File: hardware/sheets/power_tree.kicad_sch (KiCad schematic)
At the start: 0 parts

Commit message: hw: draw Rev A power tree and charger with USB charging state (#5)
* fw: add ICM-42688-P I2C driver

NCS v3.4.1's icm4268x driver supports SPI only, and the Rev A IMU is
wired for I2C. Add a small project driver, packaged as a Zephyr module
under firmware/src/drivers so the application and tests share its
Kconfig, bindings and sources.

The driver reuses the stock register map and devicetree property
encoding, applies the datasheet's I2C settings (I3C SDR/DDR off, slew
rates, SPI interface disabled) and INT_ASYNC_RESET = 0, and supports
data-ready interrupts. Moving the part to SPI only changes the node.

An emulator test on native_sim covers reset and identity checks, the
I2C-mode configuration, unit conversion and the data-ready path. It
does not prove behavior on the real part; wake-on-motion is not
implemented yet.

* hw: add regulator and charger symbols and footprints

Add TPS63802, TPS61023 and BQ25620 symbols with pins and electrical
types from TI's pin tables, and footprints drawn from the manufacturer
land patterns: TI DLA0010A, DRL0006A and RYK0018A (whose L-shaped
corner pads are two pads each), Coilcraft XEL4030 and Murata
DFE201612E.

The TPS63802 body is 2.0 x 3.0 mm per outline 4223750/D; the
datasheet's introductory 1.4 x 2.3 mm figure is out of date.

* hw: draw Rev A power tree and USB charger sheets

Power tree: TPS63802 3.3 V logic rail, TPS61023 LED rail with load
disconnect, switched VBAT measurement, VLED sense, 0-ohm measurement
links and test points. The logic rail is enabled by the power switch
or by the charger's power-good output, so USB starts a charging-only
state with the switch off and removing USB turns the rail off again.
The LED rail and VBAT measurement default off.

Charger: USB-C sink with separate 5.1 kOhm Rd, TPD4E05U06 on D+, D-,
CC1 and CC2, isolated CC sensing, BQ25620 switching charger with BC1.2
detection, a board NTC on TS, and the JST-PH battery header.

The VLED setting is provisional until LED testing. The battery he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
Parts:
- added C201, C203: 10uF 25V, Capacitor_SMD:C_0805_2012Metric, symbol Device:C
- added C202, C204, C205: 22uF 25V, Capacitor_SMD:C_0805_2012Metric, symbol Device:C
- added C206: 4.7nF, Capacitor_SMD:C_0402_1005Metric, symbol Device:C
- added C207, C208: 100nF, Capacitor_SMD:C_0402_1005Metric, symbol Device:C
- added L201: 0.47uH, smart-led-badge:L_Murata_DFE201612E, symbol Device:L
- added L202: 1uH, smart-led-badge:L_Coilcraft_XEL4030, symbol Device:L
- added Q201, Q203: AO3401A, Package_TO_SOT_SMD:SOT-23, symbol Transistor_FET:AO3401A
- added Q202, Q204: AO3400A, Package_TO_SOT_SMD:SOT-23, symbol Transistor_FET:AO3400A
- added R201: 10k, Resistor_SMD:R_0402_1005Metric, symbol Device:R
- added R202, R205: 20k, Resistor_SMD:R_0402_1005Metric, symbol Device:R
- added R203, R208, R214, R219, R222, R223: 100k, Resistor_SMD:R_0402_1005Metric, symbol Device:R
- added R204: 12k, Resistor_SMD:R_0402_1005Metric, symbol Device:R
- added R206, R207: 0, Resistor_SMD:R_0402_1005Metric, symbol Device:R
- added R209, R215: 0, Resistor_SMD:R_0805_2012Metric, symbol Device:R
- added R210: 33k, Resistor_SMD:R_0402_1005Metric, symbol Device:R
- added R211, R217: 4.7k, Resistor_SMD:R_0402_1005Metric, symbol Device:R
- added R212, R213: DNP, Resistor_SMD:R_0402_1005Metric, symbol Device:R
- added R216: 200k, Resistor_SMD:R_0402_1005Metric, symbol Device:R
- added R218, R220, R221: 47k, Resistor_SMD:R_0402_1005Metric, symbol Device:R
- added SW201: Power switch (SPDT, part TBD), symbol Switch:SW_SPDT
- added TP201: SYS, TestPoint:TestPoint_Pad_D1.0mm, symbol Connector:TestPoint
- added TP202: VBAT, TestPoint:TestPoint_Pad_D1.0mm, symbol Connector:TestPoint
- added TP203: 3V3_REG, TestPoint:TestPoint_Pad_D1.0mm, symbol Connector:TestPoint
- added TP204: +3V3, TestPoint:TestPoint_Pad_D1.0mm, symbol Connector:TestPoint
- added TP205: VLED_REG, TestPoint:TestPoint_Pad_D1.0mm, symbol Connector:TestPoint
- added TP206: VLED, TestPoint:TestPoint_Pad_D1.0mm, symbol Connector:TestPoint
- added TP207, TP208: GND, TestPoint:TestPoint_Pad_D1.0mm, symbol Connector:TestPoint
- added TP209: EN_3V3, TestPoint:TestPoint_Pad_D1.0mm, symbol Connector:TestPoint
- added TP210: PG_3V3, TestPoint:TestPoint_Pad_D1.0mm, symbol Connector:TestPoint
- added TP211: LED_EN, TestPoint:TestPoint_Pad_D1.0mm, symbol Connector:TestPoint
- added TP212: VBAT_SENSE, TestPoint:TestPoint_Pad_D1.0mm, symbol Connector:TestPoint
- added TP213: VLED_SENSE, TestPoint:TestPoint_Pad_D1.0mm, symbol Connector:TestPoint
- added TP214: VBAT_MEAS_EN, TestPoint:TestPoint_Pad_D1.0mm, symbol Connector:TestPoint
- added TP215: SW_ON, TestPoint:TestPoint_Pad_D1.0mm, symbol Connector:TestPoint
- added TP216: PWR_SW_N, TestPoint:TestPoint_Pad_D1.0mm, symbol Connector:TestPoint
- added U201: TPS63802, smart-led-badge:Texas_DLA0010A, symbol smart-led-badge:TPS63802
- added U202: TPS61023, smart-led-badge:Texas_DRL0006A, symbol smart-led-badge:TPS61023
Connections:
- new net +3V3: R209.2, TP204.1
- new net 3V3_REG: C202.1, R203.1, R207.1, R208.1, R209.1, TP203.1, U201.6 (VOUT)
- new net CHG_PG_N: Q203.1 (G), R223.2
- new net EN_3V3: Q203.3 (D), R201.2, R202.1, TP209.1, U201.1 (EN)
- new net FB_3V3: R204.2, R205.1, U201.4 (FB)
- new net FB_3V3_A: R203.2, R204.1
- new net FB_VLED: C206.2, R210.2, R211.1, R212.2, R213.1, U202.1 (FB)
- new net GND: C201.2, C202.2, C203.2, C204.2, C205.2, C207.2, C208.2, Q202.2 (S), Q204.2 (S), R202.2, R205.2, R206.2, R211.2, R213.2, R214.2, R217.2, R219.2, R221.2, R222.2, TP207.1, TP208.1, U201.3 (AGND), U201.8 (GND), U202.4 (GND)
- new net L1_3V3: L201.1, U201.9 (L1)
- new net L2_3V3: L201.2, U201.7 (L2)
- new net LED_EN: R214.1, TP211.1, U202.2 (EN)
- new net MODE_3V3: R206.1, R207.2, U201.2 (MODE)
- new net PG_3V3: R208.2, TP210.1, U201.5 (PG)
- new net PWR_SW_N: Q204.3 (D), TP216.1
- new net SW_ON: Q204.1 (G), R201.1, R222.1, SW201.1 (A), TP215.1
- new net SW_VLED: L202.2, U202.5 (SW)
- new net SYS: C201.1, C203.1, L202.1, Q203.2 (S), R223.1, SW201.2 (B), TP201.1, U201.10 (VIN), U202.3 (VIN)
- new net VBAT: Q201.2 (S), R218.1, TP202.1
- new net VBAT_MEAS_EN: Q202.1 (G), R219.1, TP214.1
- new net VBAT_SENSE: C208.1, R220.2, R221.1, TP212.1
- new net VBAT_SW: Q201.3 (D), R220.1
- new net VBAT_SW_G: Q201.1 (G), Q202.3 (D), R218.2
- new net VLED: R215.2, R216.1, TP206.1
- new net VLED_REG: C204.1, C205.1, C206.1, R210.1, R212.1, R215.1, TP205.1, U202.6 (VOUT)
- new net VLED_SENSE: C207.1, R216.2, R217.1, TP213.1
- no-connect marks 0 -> 1
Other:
- note added: "PWR_FLAG on VBAT: the battery connector drives it. PWR_FLAG on +3V3 and VLED: the rails are driven through 0-ohm measurement links. SYS is driven by the BQ25620 SYS pin (USB/charger/battery sheet)."
- note added: "Regulators and power tree (Rev A) - design notes Power states: EN_3V3 = switch ON (SYS via R201) OR charger PG (Q203). OFF + battery only: EN low, 3V3 off. OFF + valid USB: PG low -> 3V3 on for the charging-only firmware mode (display off). USB removed with the switch OFF: PG releases, R202 pulls EN low, 3V3 shuts down in hardware. EN <= SYS (< 4.6 V) < 6 V abs max. PWR_SW_N (Q204, open drain) re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"

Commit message: hw: select USB-C receptacle and power switch
Use the HRO TYPE-C-31-M-12 receptacle and the C&K PCM12SMTR right-angle
slide switch. KiCad's footprints for both match the vendor drawings,
and the switch's common terminal is on SYS as drawn.
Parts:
- SW201: value Power switch (SPDT, part TBD) -> PCM12SMTR; footprint (none) -> Button_Switch_SMD:SW_SPDT_PCM12; LCSC (none) -> C221841; MPN (none) -> PCM12SMTR; Manufacturer (none) -> C&K; Note Mechanical gate: slide switch MPN/footprint not selected -> Right-angle SPDT slide switch on the right edge; terminal 2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
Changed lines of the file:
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@@
 			)
 		)
-		(property "Value" "Power switch (SPDT, part TBD)"
+		(property "Value" "PCM12SMTR"
 			(at 27.94 66.04 0)
 			(effects
@@
 			)
 		)
-		(property "Footprint" ""
+		(property "Footprint" "Button_Switch_SMD:SW_SPDT_PCM12"
 			(at 33.02 60.96 0)
 			(hide yes)
@@
 			)
 		)
-		(property "Note" "Mechanical gate: slide switch MPN/footprint not selected"
+		(property "Manufacturer" "C&K"
 			(at 33.02 60.96 0)
 			(hide yes)
+			(effects
+				(font
+					(size 1.27 1.27)
+				)
+			)
+		)
+		(property "MPN" "PCM12SMTR"
+			(at 33.02 60.96 0)
+			(hide yes)
+			(effects
+				(font
+					(size 1.27 1.27)
+				)
+			)
+		)
+		(property "LCSC" "C221841"
+			(at 33.02 60.96 0)
+			(hide yes)
+			(effects
+				(font
+					(size 1.27 1.27)
+				)
+			)
+		)
+		(property "Note" "Right-angle SPDT slide switch on the right edge; terminal 2 common (C&K PCM series); carries uA only"
+			(at 33.02 60.96 0)
+			(hide yes)

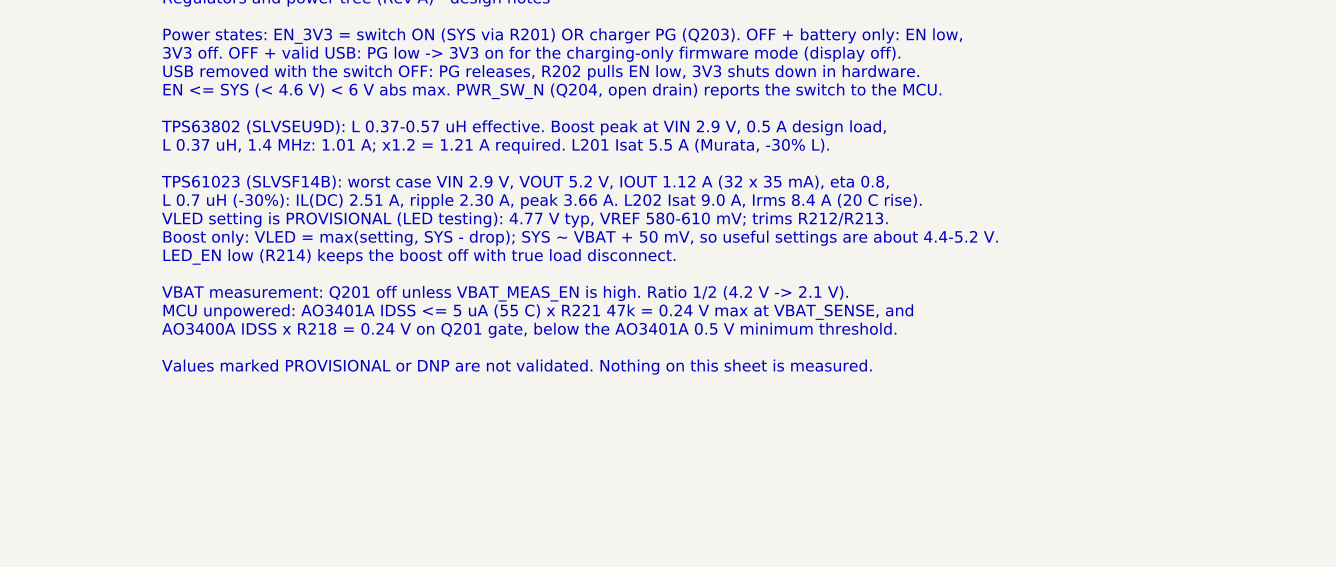
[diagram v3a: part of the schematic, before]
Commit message: hw: use 2.1 mm XGL4020 inductors for the LED rail and charger
With every part on the front, part height adds directly to the badge
thickness. The 3.1 mm XEL4030 on the LED boost (L202) and charger (L301)
becomes a Coilcraft XGL4020-102MEC, 2.10 mm max, with the same 0.98 x
3.4 mm land pattern at 2.37 mm centres.

The worst-case boost peak is 2.94 A with the 18.0 mA column cap (2.9 V
in, 5.33 V out, 0.66 A, -20 % inductance tolerance, -20 % switching
frequency), below the 3.8 A rating for a 10 % inductance drop. The
earlier 3.66 A figure assumed 35 mA columns. The charger peaks at
2.76 A at the 1.5 A input limit. Current-limit cases stay below the
30 % drop point. These are calculations, not measurements.
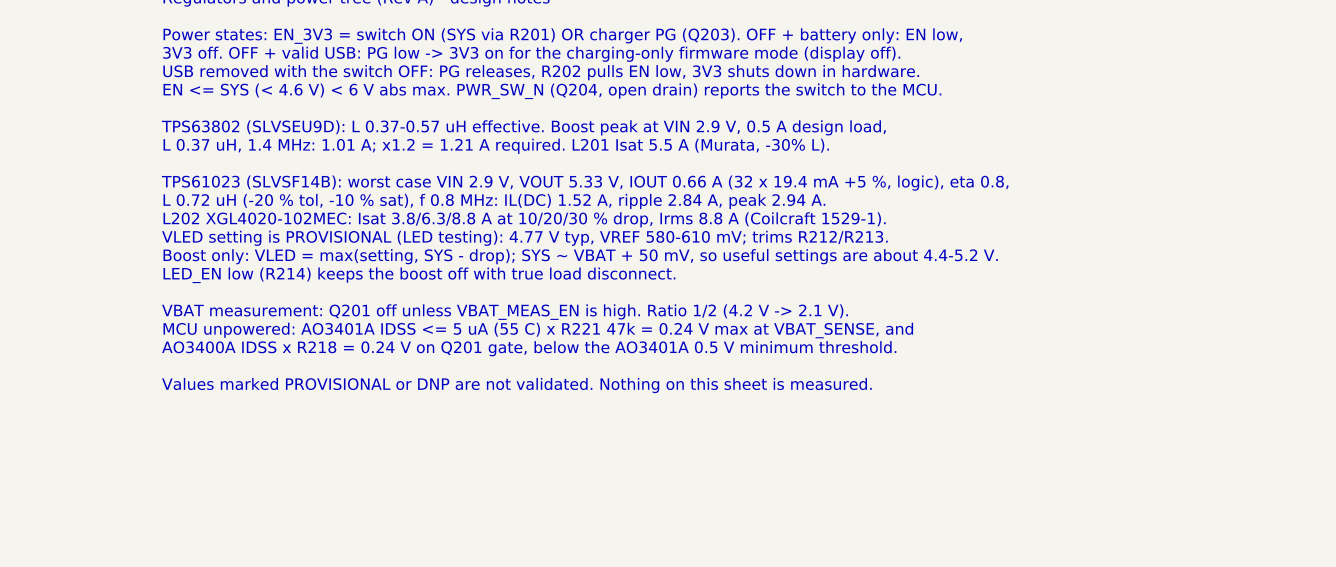
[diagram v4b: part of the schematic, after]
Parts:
- L202: footprint smart-led-badge:L_Coilcraft_XEL4030 -> smart-led-badge:L_Coilcraft_XGL4020; LCSC C5441341 -> C5357696; MPN XEL4030-102MEC -> XGL4020-102MEC
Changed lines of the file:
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@@
 		)
 	)
-	(text "Regulators and power tree (Rev A) - design notes\n\nPower states: EN_3V3 = switch ON (SYS via R201) OR charger PG (Q203). OFF + battery only: EN low,\n3V3 off. OFF + valid USB: PG low -> 3V3 on for the charging-only firmware mode (display off).\nUSB removed with the switch OFF: PG releases, R202 pulls EN low, 3V3 shuts down in hardware.\nEN <= SYS (< 4.6 V) < 6 V abs max. PWR_SW_N (Q204, open drain) reports the switch to the MCU.\n\nTPS63802 (SLVSEU9D): L 0.37-0.57 uH effective. Boost peak at VIN 2.9 V, 0.5 A design load,\nL 0.37 uH, 1.4 MHz: 1.01 A; x1.2 = 1.21 A required. L201 Isat 5.5 A (Murata, -30% L).\n\nTPS61023 (SLVSF14B): worst case VIN 2.9 V, VOUT 5.2 V, IOUT 1.12 A (32 x 35 mA), eta 0.8,\nL 0.7 uH (-30%): IL(DC) 2.51 A, ripple 2.30 A, peak 3.66 A. L202 Isat 9.0 A, Irms 8.4 A (20 C rise).\nVLED setting is PROVISIONAL (LED testing): 4.77 V typ, VREF 580-610 mV; trims R212/R213.\nBoost only: VLED = max(setting, SYS - drop); SYS ~ VBAT + 50 mV, so useful settings are about 4.4-5.2 V.\nLED_EN low (R214) keeps the boost off with true load disconnect.\n\nVBAT measurement: Q201 off unless VBAT_MEAS_EN is high. Ratio 1/2 (4.2 V -> 2.1 V).\nMCU unpowered: AO3401A IDSS <= 5 uA (55 C) x R221 47k = 0.24 V max at VBAT_SENSE, and\nAO3400A IDSS x R218 = 0.24 V on Q201 gate, below the AO3401A 0.5 V minimum threshold.\n\nValues marked PROVISIONAL or DNP are not validated. Nothing on this sheet is measured."
+	(text "Regulators and power tree (Rev A) - design notes\n\nPower states: EN_3V3 = switch ON (SYS via R201) OR charger PG (Q203). OFF + battery only: EN low,\n3V3 off. OFF + valid USB: PG low -> 3V3 on for the charging-only firmware mode (display off).\nUSB removed with the switch OFF: PG releases, R202 pulls EN low, 3V3 shuts down in hardware.\nEN <= SYS (< 4.6 V) < 6 V abs max. PWR_SW_N (Q204, open drain) reports the switch to the MCU.\n\nTPS63802 (SLVSEU9D): L 0.37-0.57 uH effective. Boost peak at VIN 2.9 V, 0.5 A design load,\nL 0.37 uH, 1.4 MHz: 1.01 A; x1.2 = 1.21 A required. L201 Isat 5.5 A (Murata, -30% L).\n\nTPS61023 (SLVSF14B): worst case VIN 2.9 V, VOUT 5.33 V, IOUT 0.66 A (32 x 19.4 mA +5 %, logic), eta 0.8,\nL 0.72 uH (-20 % tol, -10 % sat), f 0.8 MHz: IL(DC) 1.52 A, ripple 2.84 A, peak 2.94 A.\nL202 XGL4020-102MEC: Isat 3.8/6.3/8.8 A at 10/20/30 % drop, Irms 8.8 A (Coilcraft 1529-1).\nVLED setting is PROVISIONAL (LED testing): 4.77 V typ, VREF 580-610 mV; trims R212/R213.\nBoost only: VLED = max(setting, SYS - drop); SYS ~ VBAT + 50 mV, so useful settings are about 4.4-5.2 V.\nLED_EN low (R214) keeps the boost off with true load disconnect.\n\nVBAT measurement: Q201 off unless VBAT_MEAS_EN is high. Ratio 1/2 (4.2 V -> 2.1 V).\nMCU unpowered: AO3401A IDSS <= 5 uA (55 C) x R221 47k = 0.24 V max at VBAT_SENSE, and\nAO3400A IDSS x R218 = 0.24 V on Q201 gate, below the AO3401A 0.5 V minimum threshold.\n\nValues marked PROVISIONAL or DNP are not validated. Nothing on this sheet is measured."
 		(exclude_from_sim no)
 		(at 299.72 152.4 0)
@@
 			)
 		)
-		(property "Footprint" "smart-led-badge:L_Coilcraft_XEL4030"
+		(property "Footprint" "smart-led-badge:L_Coilcraft_XGL4020"
 			(at 101.6 99.06 0)
 			(hide yes)
@@
 			)
 		)
-		(property "MPN" "XEL4030-102MEC"
+		(property "MPN" "XGL4020-102MEC"
 			(at 101.6 99.06 0)
 			(hide yes)
@@
 			)
 		)
-		(property "LCSC" "C5441341"
+		(property "LCSC" "C5357696"
 			(at 101.6 99.06 0)
 			(hide yes)
